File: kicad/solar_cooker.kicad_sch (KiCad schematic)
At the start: 1 part

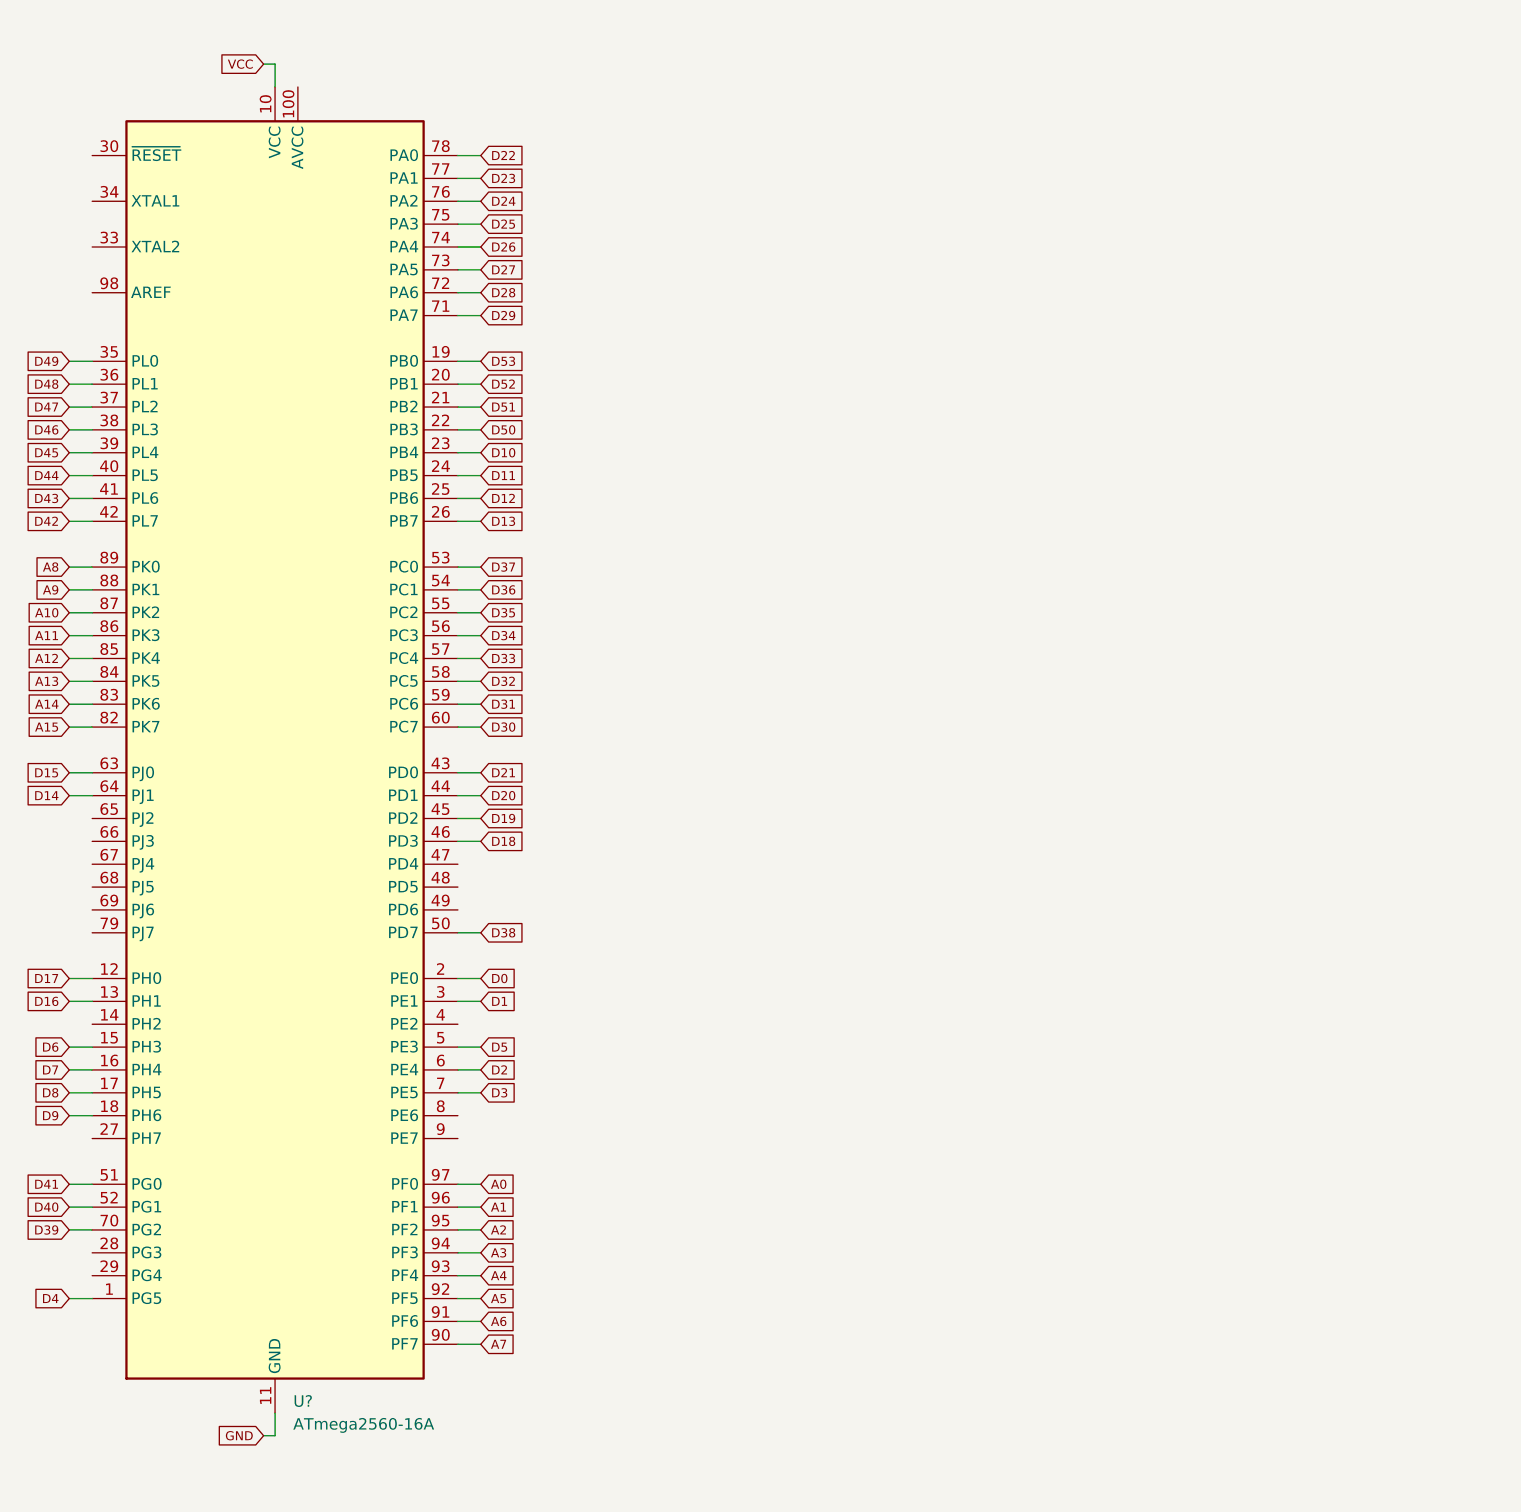
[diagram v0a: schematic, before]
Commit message: added custom microSD component
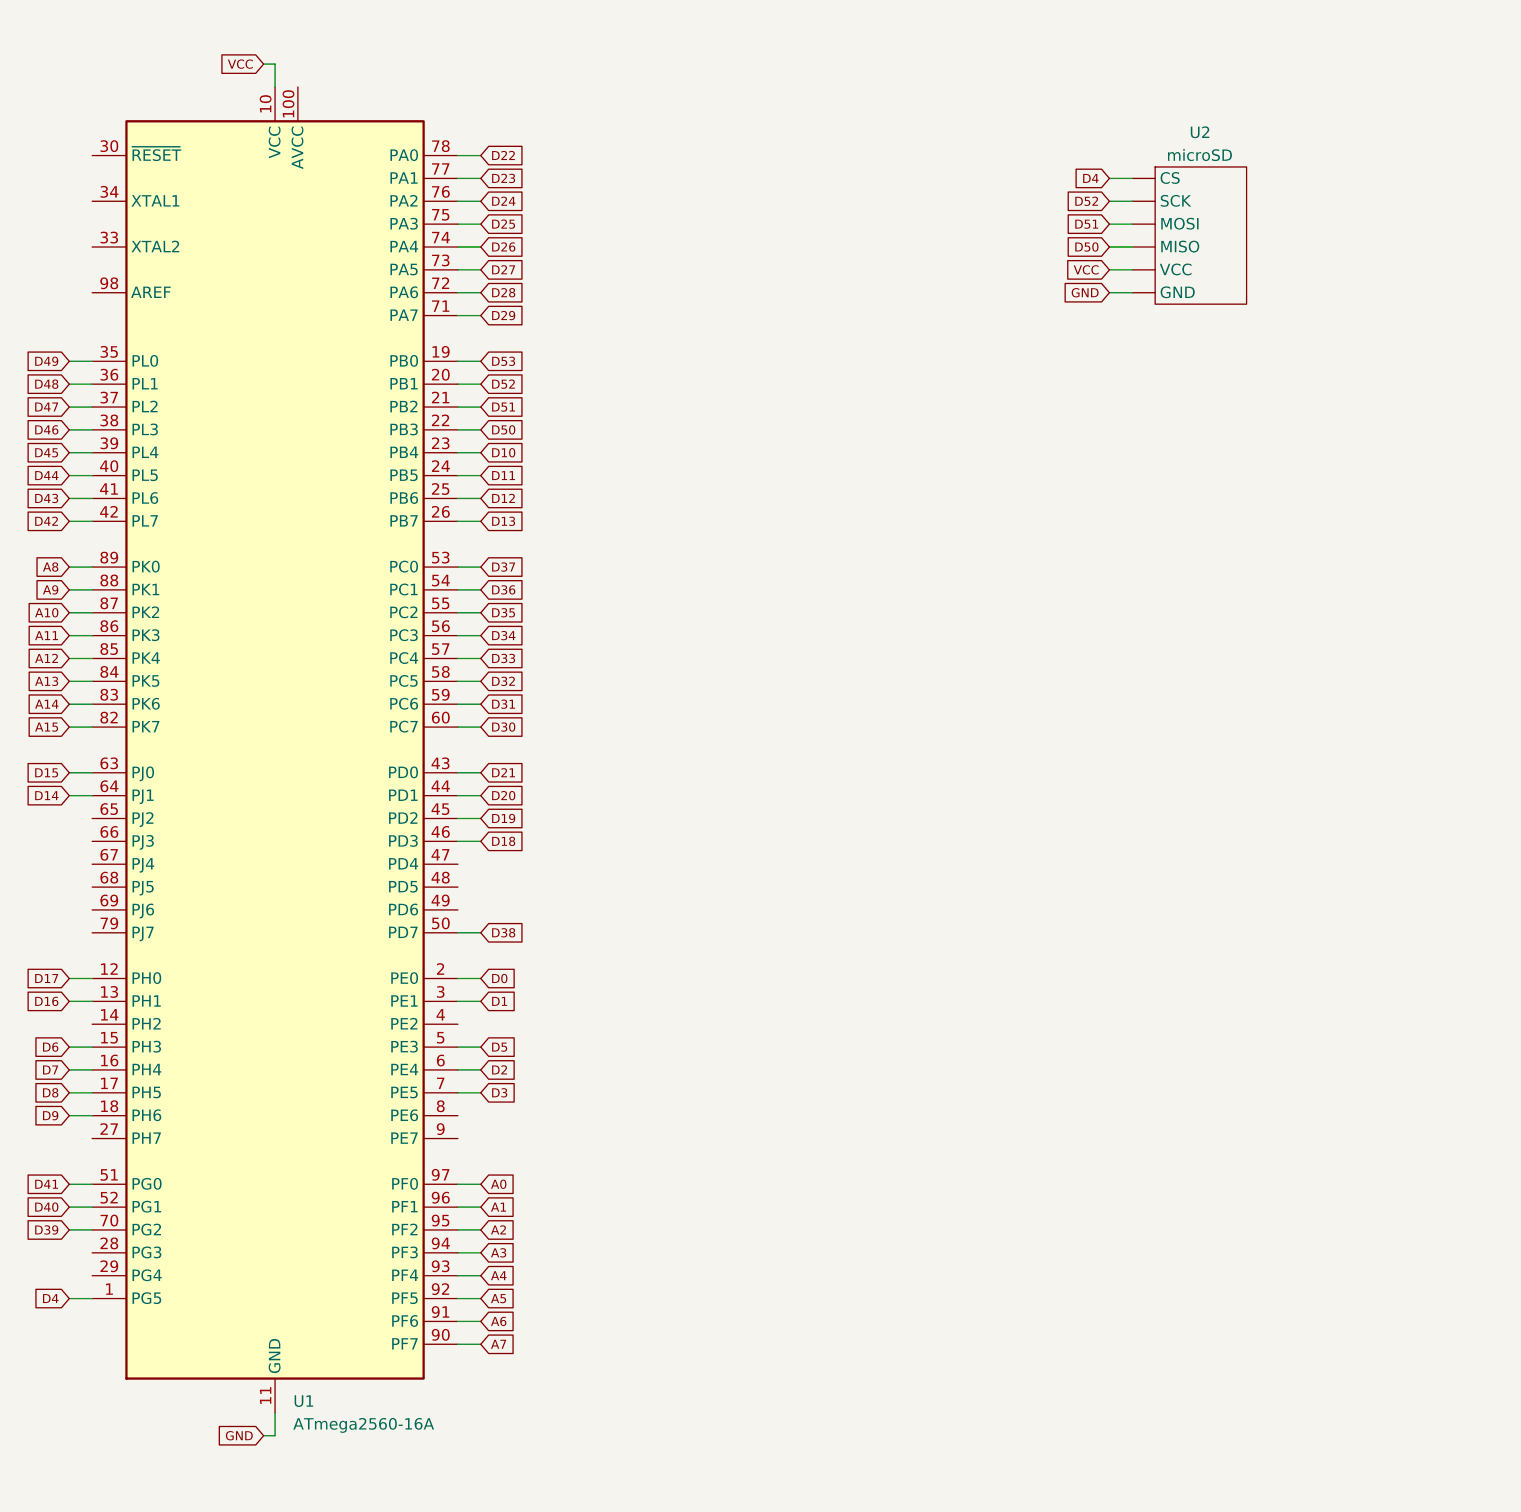
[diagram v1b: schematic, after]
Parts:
- added U2: microSD, symbol custom_components:microSD
- gave numbers to parts that had none: 1
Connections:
- net D4: now also U2. (VCC)
- net D50: now also U2. (VCC)
- net D51: now also U2. (VCC)
- net D52: now also U2. (VCC)
- net GND: now also U2. (VCC)
- net VCC: now also U2. (VCC)
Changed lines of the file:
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@@
+    (stroke (width 0) (type default) (color 0 0 255 1))
+  )
+  (wire (pts (xy 157.48 46.99) (xy 160.02 46.99))
     (stroke (width 0) (type default) (color 0 0 255 1))
   )
@@
     (stroke (width 0) (type default) (color 0 0 255 1))
   )
+  (wire (pts (xy 157.48 44.45) (xy 160.02 44.45))
+    (stroke (width 0) (type default) (color 0 0 255 1))
+  )
   (wire (pts (xy 41.91 54.61) (xy 44.45 54.61))
     (stroke (width 0) (type default) (color 0 0 255 1))
   )
+  (wire (pts (xy 157.48 39.37) (xy 160.02 39.37))
+    (stroke (width 0) (type default) (color 0 0 255 1))
+  )
   (wire (pts (xy 85.09 107.95) (xy 87.63 107.95))
     (stroke (width 0) (type default) (color 0 0 255 1))
@@
     (stroke (width 0) (type default) (color 0 0 255 1))
   )
+  (wire (pts (xy 157.48 36.83) (xy 160.02 36.83))
+    (stroke (width 0) (type default) (color 0 0 255 1))
+  )
   (wire (pts (xy 85.09 123.19) (xy 87.63 123.19))
     (stroke (width 0) (type default) (color 0 0 255 1))
@@
     (stroke (width 0) (type default) (color 0 0 0 0))
   )
+  (wire (pts (xy 157.48 34.29) (xy 160.02 34.29))
+    (stroke (width 0) (type default) (color 0 0 255 1))
+  )
   (wire (pts (xy 41.91 158.75) (xy 44.45 158.75))
     (stroke (width 0) (type default) (color 0 0 255 1))
@@
   )
   (wire (pts (xy 85.09 105.41) (xy 87.63 105.41))
+    (stroke (width 0) (type default) (color 0 0 255 1))
+  )
+  (wire (pts (xy 157.48 41.91) (xy 160.02 41.91))
     (stroke (width 0) (type default) (color 0 0 255 1))
   )
@@
     )
   )
+  (global_label "D4" (shape input) (at 157.48 34.29 180) (fields_autoplaced)
+    (effects (font (size 1 1)) (justify right))
+    (property "Intersheet References" "${INTERSHEET_REFS}" (id 0) (at 153.6276 34.2275 0)
+      (effects (font (size 1 1)) (justify right) hide)
+    )
+  )
   (global_label "D45" (shape input) (at 41.91 64.77 180) (fields_autoplaced)
     (effects (font (size 1 1)) (justify right))
@@
     )
   )
+  (global_label "D51" (shape input) (at 157.48 39.37 180) (fields_autoplaced)
+    (effects (font (size 1 1)) (justify right))
+    (property "Intersheet References" "${INTERSHEET_REFS}" (id 0) (at 152.6752 39.3075 0)
+      (effects (font (size 1 1)) (justify right) hide)
+    )
+  )
   (global_label "D47" (shape input) (at 41.91 59.69 180) (fields_autoplaced)
     (effects (font (size 1 1)) (justify right))
@@
     )
   )
+  (global_label "D52" (shape input) (at 157.48 36.83 180) (fields_autoplaced)
+    (effects (font (size 1 1)) (justify right))
+    (property "Intersheet References" "${INTERSHEET_REFS}" (id 0) (at 152.6752 36.7675 0)
+      (effects (font (size 1 1)) (justify right) hide)
+    )
+  )
   (global_label "D28" (shape input) (at 87.63 46.99 0) (fields_autoplaced)
     (effects (font (size 1 1)) (justify left))
@@
     )
   )
+  (global_label "VCC" (shape input) (at 157.48 44.45 180) (fields_autoplaced)
+    (effects (font (size 1 1)) (justify right))
+    (property "Intersheet References" "${INTERSHEET_REFS}" (id 0) (at 152.7229 44.3875 0)
+      (effects (font (size 1 1)) (justify right) hide)
+    )
+  )
   (global_label "D0" (shape input) (at 87.63 123.19 0) (fields_autoplaced)
     (effects (font (size 1 1)) (justify left))
@@
     )
   )
+  (global_label "D50" (shape input) (at 157.48 41.91 180) (fields_autoplaced)
+    (effects (font (size 1 1)) (justify right))
+    (property "Intersheet References" "${INTERSHEET_REFS}" (id 0) (at 152.6752 41.8475 0)
+      (effects (font (size 1 1)) (justify right) hide)
+    )
+  )
   (global_label "D14" (shape input) (at 41.91 102.87 180) (fields_autoplaced)
     (effects (font (size 1 1)) (justify right))
@@
     (effects (font (size 1 1)) (justify right))
     (property "Intersheet References" "${INTERSHEET_REFS}" (id 0) (at 37.1052 57.0875 0)
+      (effects (font (size 1 1)) (justify right) hide)
+    )
+  )
+  (global_label "GND" (shape input) (at 157.48 46.99 180) (fields_autoplaced)
+    (effects (font (size 1 1)) (justify right))
+    (property "Intersheet References" "${INTERSHEET_REFS}" (id 0) (at 152.5324 46.9275 0)
       (effects (font (size 1 1)) (justify right) hide)
     )
@@
   (symbol (lib_id "MCU_Microchip_ATmega:ATmega2560-16A") (at 64.77 97.79 0) (unit 1)
     (in_bom yes) (on_board yes) (fields_autoplaced)
-    (property "Reference" "U?" (id 0) (at 66.7894 170.18 0)
+    (property "Reference" "U1" (id 0) (at 66.7894 170.18 0)
       (effects (font (size 1.27 1.27)) (justify left))
     )
@@
     (pin "99")
   )
+  (symbol (lib_id "custom_components:microSD") (at 167.64 40.64 0) (unit 1)
+    (in_bom yes) (on_board yes)
+    (property "Reference" "U2" (id 0) (at 166.37 29.21 0)
+      (effects (font (size 1.27 1.27)) (justify left))
+    )
+    (property "Value" "microSD" (id 1) (at 163.83 31.75 0)
+      (effects (font (size 1.27 1.27)) (justify left))
+    )
+    (property "Footprint" "" (id 2) (at 167.64 40.64 0)
+      (effects (font (size 1.27 1.27)) hide)
+    )
+    (property "Datasheet" "" (id 3) (at 167.64 40.64 0)
+      (effects (font (size 1.27 1.27)) hide)
+    )
+    (pin "")
+    (pin "")
+    (pin "")
+    (pin "")
+    (pin "")
+    (pin "")
+  )
   (sheet_instances
     (path "/" (page "1"))
@@
   (symbol_instances
     (path "/86a35b78-d9bc-4866-8086-f681ae9cfe0c"
-      (reference "U?") (unit 1) (value "ATmega2560-16A") (footprint "Package_QFP:TQFP-100_14x14mm_P0.5mm")
-    )
-  )
+      (reference "U1") (unit 1) (value "ATmega2560-16A") (footprint "Package_QFP:TQFP-100_14x14mm_P0.5mm")
+    )
+    (path "/9e138a49-51b8-4d1f-9918-656981834e6d"
+      (reference "U2") (unit 1) (value "microSD") (footprint "")
+    )
+  )

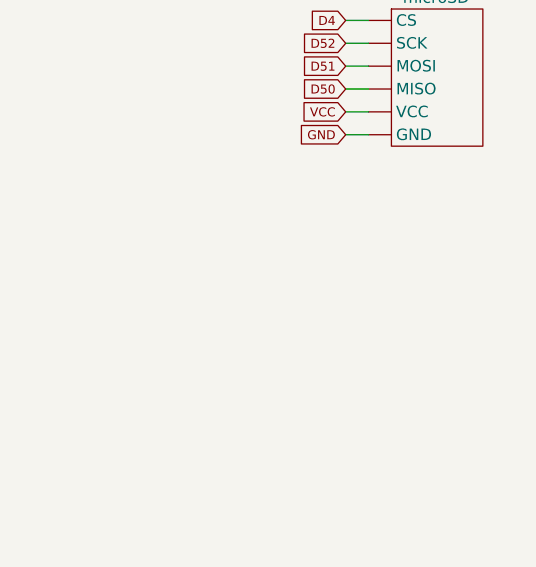
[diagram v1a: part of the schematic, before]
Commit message: added clockModule
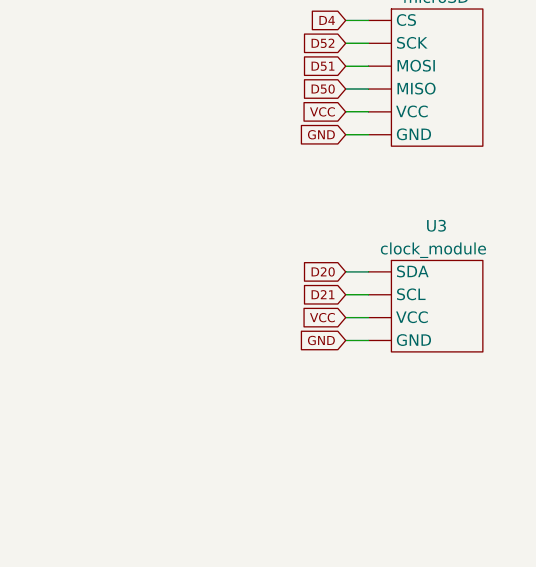
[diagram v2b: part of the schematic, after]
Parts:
- added U3: clock_module, symbol custom_components:clock_module
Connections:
- net D20: now also U3. (VCC)
- net D21: now also U3. (VCC)
- net GND: now also U3. (VCC)
- net VCC: now also U3. (VCC)
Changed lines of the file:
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@@
   )
   (wire (pts (xy 157.48 46.99) (xy 160.02 46.99))
+    (stroke (width 0) (type default) (color 0 0 0 1))
+  )
+  (wire (pts (xy 157.48 62.23) (xy 160.02 62.23))
     (stroke (width 0) (type default) (color 0 0 255 1))
   )
@@
     (stroke (width 0) (type default) (color 0 0 255 1))
   )
+  (wire (pts (xy 157.48 69.85) (xy 160.02 69.85))
+    (stroke (width 0) (type default) (color 0 0 0 1))
+  )
   (wire (pts (xy 64.77 171.45) (xy 64.77 173.99))
     (stroke (width 0) (type default) (color 0 0 0 1))
@@
   )
   (wire (pts (xy 157.48 44.45) (xy 160.02 44.45))
-    (stroke (width 0) (type default) (color 0 0 255 1))
+    (stroke (width 0) (type default) (color 255 0 0 1))
   )
   (wire (pts (xy 41.91 54.61) (xy 44.45 54.61))
@@
   (wire (pts (xy 85.09 148.59) (xy 87.63 148.59))
     (stroke (width 0) (type default) (color 0 0 0 0))
+  )
+  (wire (pts (xy 157.48 67.31) (xy 160.02 67.31))
+    (stroke (width 0) (type default) (color 255 0 0 1))
+  )
+  (wire (pts (xy 157.48 64.77) (xy 160.02 64.77))
+    (stroke (width 0) (type default) (color 0 0 255 1))
   )
   (wire (pts (xy 85.09 80.01) (xy 87.63 80.01))
@@
     )
   )
+  (global_label "GND" (shape input) (at 157.48 69.85 180) (fields_autoplaced)
+    (effects (font (size 1 1)) (justify right))
+    (property "Intersheet References" "${INTERSHEET_REFS}" (id 0) (at 152.5324 69.7875 0)
+      (effects (font (size 1 1)) (justify right) hide)
+    )
+  )
   (global_label "D46" (shape input) (at 41.91 62.23 180) (fields_autoplaced)
     (effects (font (size 1 1)) (justify right))
@@
     )
   )
+  (global_label "D21" (shape input) (at 157.48 64.77 180) (fields_autoplaced)
+    (effects (font (size 1 1)) (justify right))
+    (property "Intersheet References" "${INTERSHEET_REFS}" (id 0) (at 152.6752 64.7075 0)
+      (effects (font (size 1 1)) (justify right) hide)
+    )
+  )
+  (global_label "VCC" (shape input) (at 157.48 67.31 180) (fields_autoplaced)
+    (effects (font (size 1 1)) (justify right))
+    (property "Intersheet References" "${INTERSHEET_REFS}" (id 0) (at 152.7229 67.2475 0)
+      (effects (font (size 1 1)) (justify right) hide)
+    )
+  )
   (global_label "D48" (shape input) (at 41.91 57.15 180) (fields_autoplaced)
     (effects (font (size 1 1)) (justify right))
@@
     (property "Intersheet References" "${INTERSHEET_REFS}" (id 0) (at 92.4348 59.6275 0)
       (effects (font (size 1 1)) (justify left) hide)
+    )
+  )
+  (global_label "D20" (shape input) (at 157.48 62.23 180) (fields_autoplaced)
+    (effects (font (size 1 1)) (justify right))
+    (property "Intersheet References" "${INTERSHEET_REFS}" (id 0) (at 152.6752 62.1675 0)
+      (effects (font (size 1 1)) (justify right) hide)
     )
   )
@@
     (pin "")
   )
+  (symbol (lib_id "custom_components:clock_module") (at 167.64 66.04 0) (unit 1)
+    (in_bom yes) (on_board yes)
+    (property "Reference" "U3" (id 0) (at 166.37 57.15 0)
+      (effects (font (size 1.27 1.27)) (justify left))
+    )
+    (property "Value" "clock_module" (id 1) (at 161.29 59.69 0)
+      (effects (font (size 1.27 1.27)) (justify left))
+    )
+    (property "Footprint" "" (id 2) (at 167.64 66.04 0)
+      (effects (font (size 1.27 1.27)) hide)
+    )
+    (property "Datasheet" "" (id 3) (at 167.64 66.04 0)
+      (effects (font (size 1.27 1.27)) hide)
+    )
+    (pin "")
+    (pin "")
+    (pin "")
+    (pin "")
+  )
   (sheet_instances
     (path "/" (page "1"))
@@
       (reference "U2") (unit 1) (value "microSD") (footprint "")
     )
-  )
+    (path "/d1fef1d0-d713-4c4b-b9ac-2c34b840978b"
+      (reference "U3") (unit 1) (value "clock_module") (footprint "")
+    )
+  )
